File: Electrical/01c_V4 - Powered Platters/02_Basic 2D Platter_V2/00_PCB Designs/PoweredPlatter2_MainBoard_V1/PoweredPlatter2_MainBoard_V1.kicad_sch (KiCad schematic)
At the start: 0 parts

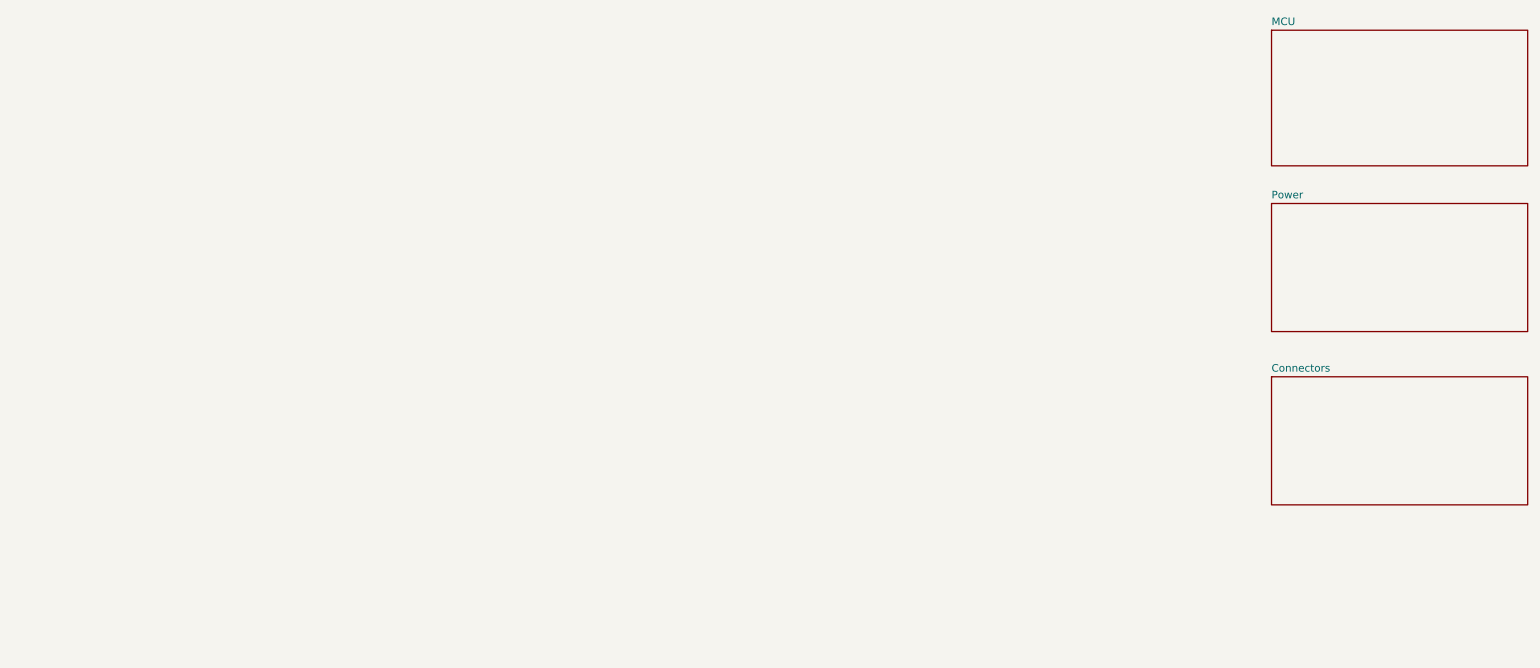
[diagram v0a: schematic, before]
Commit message: ignore kicad .history folders -messes with git of overall project
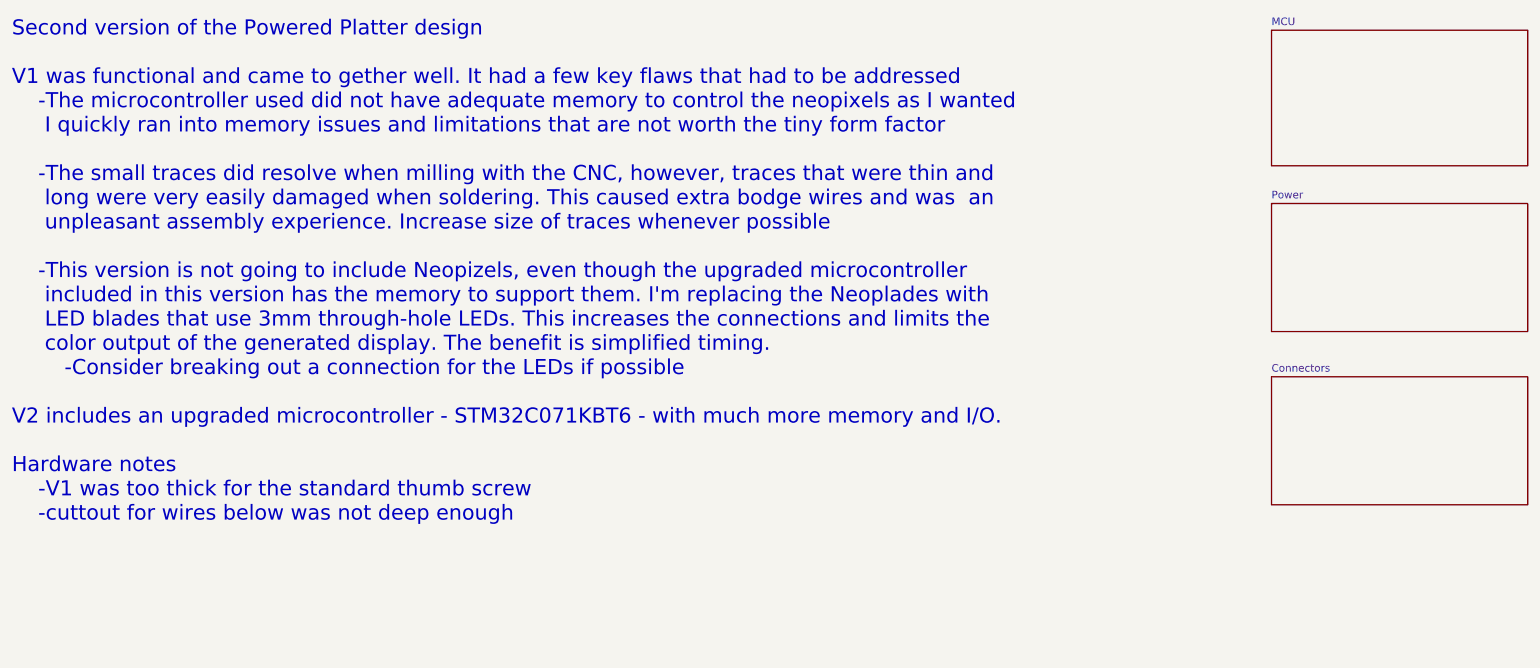
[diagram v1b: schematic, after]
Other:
- note added: "Second version of the Powered Platter design V1 was functional and came to gether well. It had a few key flaws that had to be addressed -The microcontroller used did not have adequate memory to control the neopixels as I wanted I quickly ran into memory issues and limitations that are not worth the tiny form factor -The small traces did resolve when milling with the CNC, however, traces that were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"
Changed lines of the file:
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@@
 	(generator_version "10.0")
 	(paper "A4")
+	(text "Second version of the Powered Platter design\n\nV1 was functional and came to gether well. It had a few key flaws that had to be addressed\n	-The microcontroller used did not have adequate memory to control the neopixels as I wanted\n	 I quickly ran into memory issues and limitations that are not worth the tiny form factor\n\n	-The small traces did resolve when milling with the CNC, however, traces that were thin and\n	 long were very easily damaged when soldering. This caused extra bodge wires and was  an \n	 unpleasant assembly experience. Increase size of traces whenever possible\n\n	-This version is not going to include Neopizels, even though the upgraded microcontroller\n	 included in this version has the memory to support them. I'm replacing the Neoplades with\n	 LED blades that use 3mm through-hole LEDs. This increases the connections and limits the\n	 color output of the generated display. The benefit is simplified timing.\n		-Consider breaking out a connection for the LEDs if possible\n\nV2 includes an upgraded microcontroller - STM32C071KBT6 - with much more memory and I/O. \n\nHardware notes\n	-V1 was too thick for the standard thumb screw\n	-cuttout for wires below was not deep enough"
+		(exclude_from_sim no)
+		(at 21.336 104.648 0)
+		(effects
+			(font
+				(size 2.54 2.54)
+				(thickness 0.25)
+			)
+			(justify left bottom)
+		)
+	)
 	(sheet
 		(at 233.68 50.8)

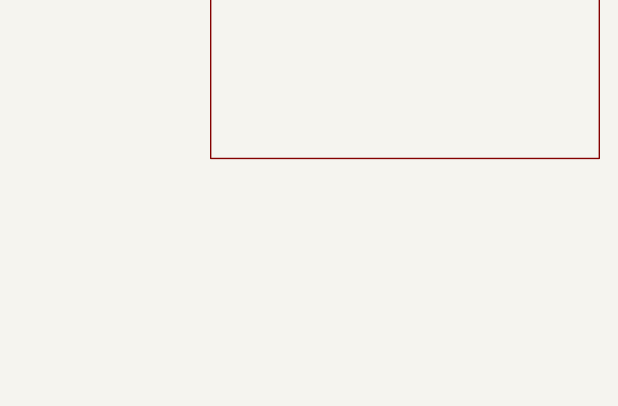
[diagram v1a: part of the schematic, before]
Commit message: second powered platter main PCB designed and ready for CNC milling
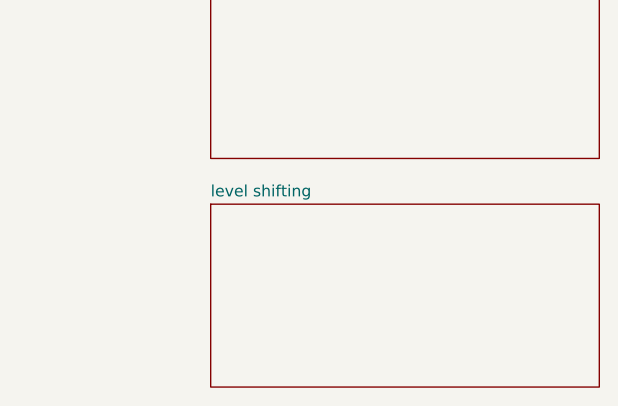
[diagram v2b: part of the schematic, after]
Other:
- added sheet level shifting (level shifting.kicad_sch)
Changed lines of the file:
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@@
+	)
+	(sheet
+		(at 233.68 106.68)
+		(size 43.18 20.32)
+		(exclude_from_sim no)
+		(in_bom yes)
+		(on_board yes)
+		(dnp no)
+		(fields_autoplaced yes)
+		(stroke
+			(width 0.1524)
+			(type solid)
+		)
+		(fill
+			(color 0 0 0 0)
+		)
+		(property "Sheetname" "level shifting"
+			(at 233.68 105.9684 0)
+			(show_name no)
+			(do_not_autoplace no)
+			(effects
+				(font
+					(size 1.27 1.27)
+				)
+				(justify left bottom)
+			)
+		)
+		(property "Sheetfile" "level shifting.kicad_sch"
+			(at 233.68 127.5846 0)
+			(hide yes)
+			(show_name no)
+			(do_not_autoplace no)
+			(effects
+				(font
+					(size 1.27 1.27)
+				)
+				(justify left top)
+			)
+		)
+		(instances
+			(project "PoweredPlatter2_MainBoard_V1"
+				(path "/0761a9b3-5f4b-4c5f-af4c-9bc817d3be21"
+					(page "5")
+				)
+			)
+		)
 	)
 	(sheet
